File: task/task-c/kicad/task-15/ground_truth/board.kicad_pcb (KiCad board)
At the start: 2 copper layers, 80 x 60 mm, 7 parts, among them U3 MCU

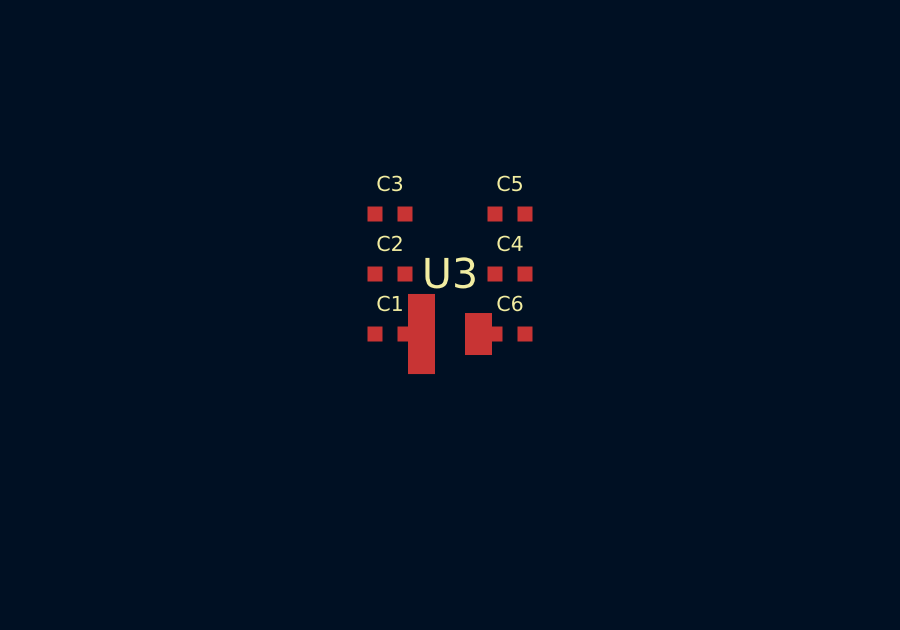
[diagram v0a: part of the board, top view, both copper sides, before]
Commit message: Fix KiCad and Blender ground-truth evaluation
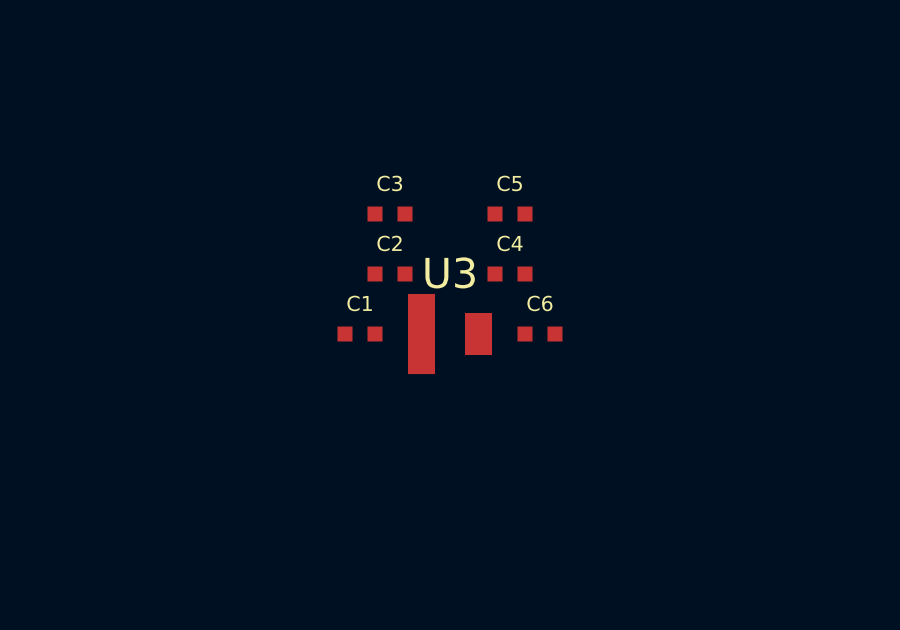
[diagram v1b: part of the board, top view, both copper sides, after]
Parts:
- C3: value 100nF -> 10uF
- C4: value 1uF -> 10uF
- moved C1 1.00 mm to (37.0, 30.0)
- moved C6 1.00 mm to (43.0, 30.0)
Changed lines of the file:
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@@
     (pad "3" smd rect (at 0.95 0) (size 0.9 1.4) (layers "F.Cu" "F.Mask") (net 1 "3V3"))
   )
-  ; C1: original 100nF cap (unchanged)
-  (footprint "C_0402" (layer "F.Cu") (at 38 30)
+  ; C1: original 100nF cap, shifted left to clear U3
+  (footprint "C_0402" (layer "F.Cu") (at 37 30)
     (fp_text reference "C1" (at 0 -1) (layer "F.Silkscreen") (effects (font (size 0.5 0.5))))
     (fp_text value "100nF" (at 0 1) (layer "F.Fab") (effects (font (size 0.5 0.5))))
@@
     (pad "2" smd rect (at 0.5 0) (size 0.5 0.5) (layers "F.Cu" "F.Mask") (net 2 "GND"))
   )
-  ; C3: additional 100nF — mid frequency, at (38, 26)
+  ; C3: additional 10uF for low-frequency impedance, at (38, 26)
   (footprint "C_0402" (layer "F.Cu") (at 38 26)
     (fp_text reference "C3" (at 0 -1) (layer "F.Silkscreen") (effects (font (size 0.5 0.5))))
-    (fp_text value "100nF" (at 0 1) (layer "F.Fab") (effects (font (size 0.5 0.5))))
+    (fp_text value "10uF" (at 0 1) (layer "F.Fab") (effects (font (size 0.5 0.5))))
     (pad "1" smd rect (at -0.5 0) (size 0.5 0.5) (layers "F.Cu" "F.Mask") (net 1 "3V3"))
     (pad "2" smd rect (at 0.5 0) (size 0.5 0.5) (layers "F.Cu" "F.Mask") (net 2 "GND"))
   )
-  ; C4: 1uF — mid-to-high frequency, at (42, 28)
+  ; C4: additional 10uF for low-frequency impedance, at (42, 28)
   (footprint "C_0402" (layer "F.Cu") (at 42 28)
     (fp_text reference "C4" (at 0 -1) (layer "F.Silkscreen") (effects (font (size 0.5 0.5))))
-    (fp_text value "1uF" (at 0 1) (layer "F.Fab") (effects (font (size 0.5 0.5))))
+    (fp_text value "10uF" (at 0 1) (layer "F.Fab") (effects (font (size 0.5 0.5))))
     (pad "1" smd rect (at -0.5 0) (size 0.5 0.5) (layers "F.Cu" "F.Mask") (net 1 "3V3"))
     (pad "2" smd rect (at 0.5 0) (size 0.5 0.5) (layers "F.Cu" "F.Mask") (net 2 "GND"))
@@
     (pad "2" smd rect (at 0.5 0) (size 0.5 0.5) (layers "F.Cu" "F.Mask") (net 2 "GND"))
   )
-  ; C6: 10nF — high frequency, at (42, 30)
-  (footprint "C_0402" (layer "F.Cu") (at 42 30)
+  ; C6: 10nF — high frequency, at (43, 30)
+  (footprint "C_0402" (layer "F.Cu") (at 43 30)
     (fp_text reference "C6" (at 0 -1) (layer "F.Silkscreen") (effects (font (size 0.5 0.5))))
     (fp_text value "10nF" (at 0 1) (layer "F.Fab") (effects (font (size 0.5 0.5))))
